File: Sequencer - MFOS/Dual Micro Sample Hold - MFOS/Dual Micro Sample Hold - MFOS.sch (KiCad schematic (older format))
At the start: 80 parts, among them J1 +12V_Conn, J10 TRIG_A, J11 CV_OUT_A, J12 GLIDE_OUT_A, J13 IN_B, J14 SampRate_1W_B, J15 SampRate_3_B, J16 LED_B, J17 Glide_1W_B, J18 Glide_3_B, J19 TRIG_B, J2 GND_Conn, J20 CV_OUT_B, J21 GLIDE_OUT_B, J3 -12V_Conn, J4 IN_A, J5 SampRate_1W_A, J6 SampRate_3_A, J7 LED_A, J8 Glide_1W_A, J9 Glide_3_A, Q1 Q_NJFET_DSG, Q2 Q_NJFET_DSG, U1 LF444, U2 LF444

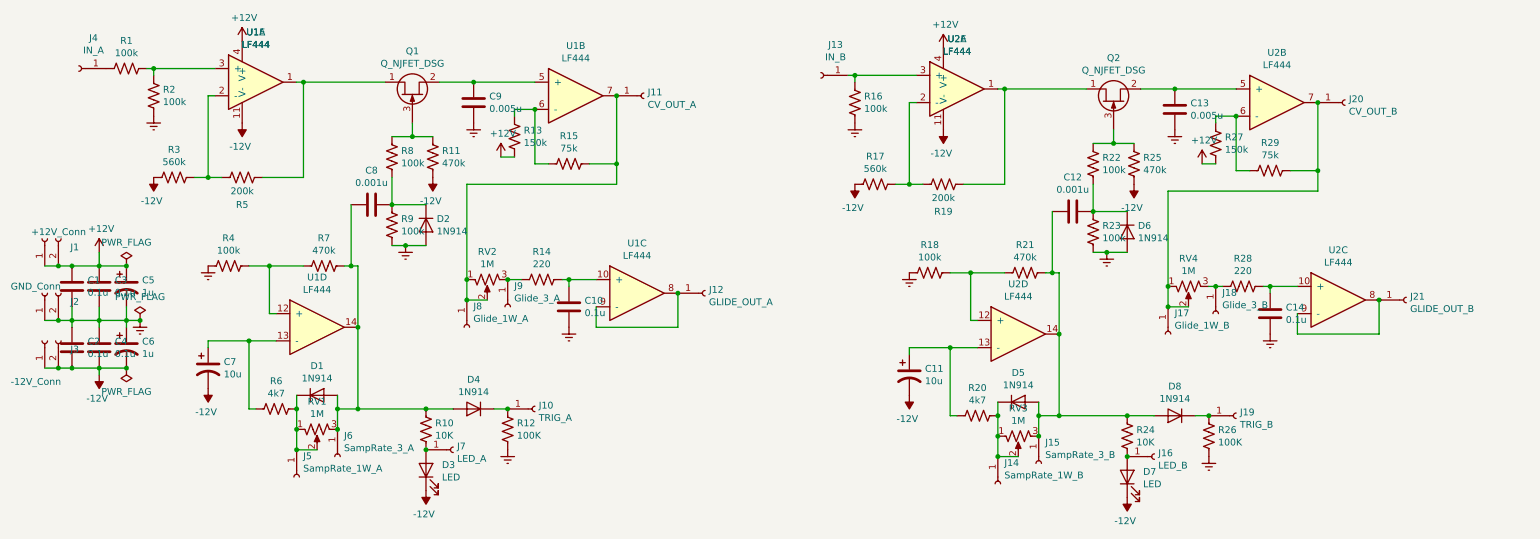
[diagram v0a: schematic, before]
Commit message: sample hold pcb added
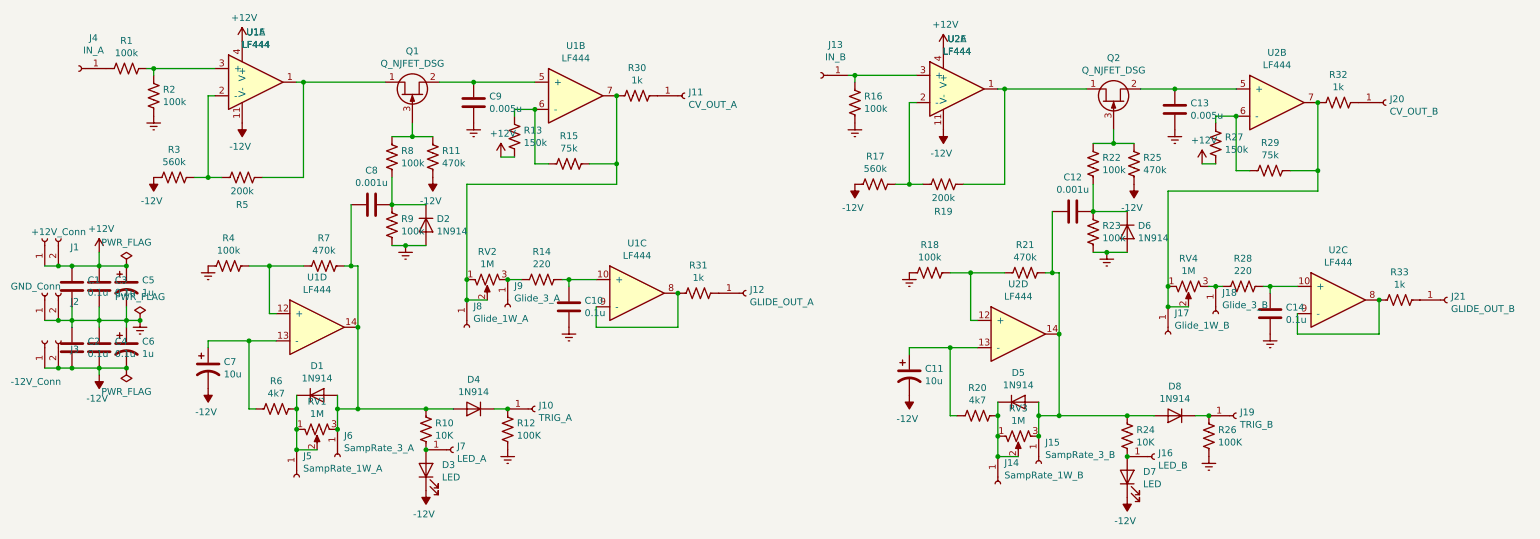
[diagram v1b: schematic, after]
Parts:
- added R30, R31, R32, R33: 1k, Resistor_THT:R_Axial_DIN0207_L6.3mm_D2.5mm_P7.62mm_Horizontal, symbol Device:R_US
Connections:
- net at J8.1 (Pin_1), R15.1, RV2.1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: now also R30.1; no longer J11.1 (Pin_1)
- net at U1.8, U1.9 (-): now also R31.1; no longer J12.1 (Pin_1)
- net at J17.1 (Pin_1), R29.1, RV4.1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: now also R32.2; no longer J20.1 (Pin_1)
- net at U2.8, U2.9 (-): now also R33.2; no longer J21.1 (Pin_1)
- new net: J12.1 (Pin_1), R31.2
- new net: J11.1 (Pin_1), R30.2
- new net: J21.1 (Pin_1), R33.1
- new net: J20.1 (Pin_1), R32.1
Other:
- moved on the sheet: J11, J12, J20, J21
